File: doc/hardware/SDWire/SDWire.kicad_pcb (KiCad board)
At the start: 2 copper layers, 21.6 x 48.4 mm, 82 parts, among them J1 usd-plug, J2 uSD Socket, P1 USB_OTG_MICRO_USB, Q3 MMBT4403LT1, Q4 MMBT4403LT1, U1 USB2640-HZH-02, U2 SPX3819M5, U3 FT200XD, U4 MC74HC1G04DTT1G, U5 TS3A27518EPWR, Y1 24MHz

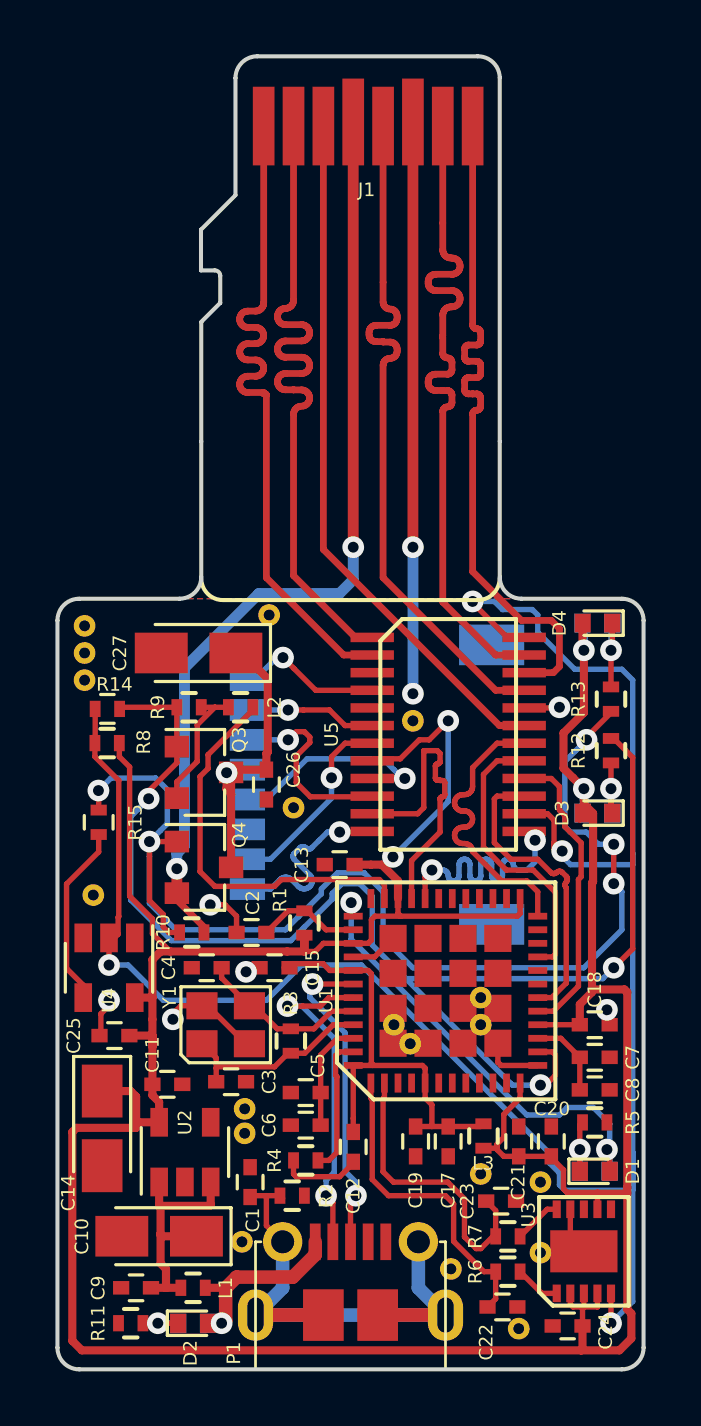
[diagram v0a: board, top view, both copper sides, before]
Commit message: Fix LEDs and card detect connections
Change-Id: I041ff52d267cebffd98fdaa6a1c2b5b6e2d7bece
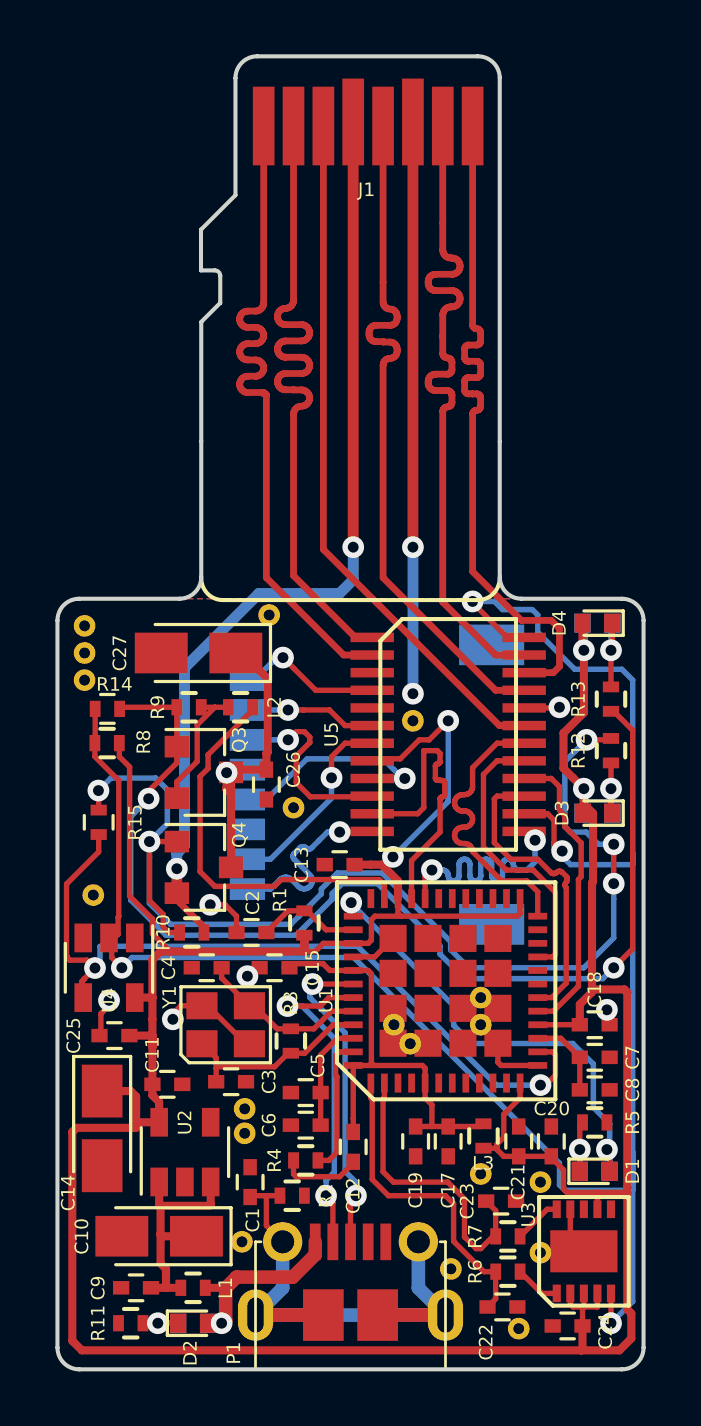
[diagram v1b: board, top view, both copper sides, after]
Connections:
- Q3 pad 1: /~CD_TS -> Net-(Q3-Pad1)
- R12 pad 2: /~CD_TS -> Net-(Q4-Pad1)
- R13 pad 2: Net-(Q4-Pad1) -> Net-(Q3-Pad1)
- R14 pad 1: /~CD_TS -> Net-(Q3-Pad1)
- R15 pad 2: Net-(R15-Pad2) -> /~CD_TS
- R9 pad 1: /~CD_TS -> Net-(Q3-Pad1)
- U4 pad 4: Net-(R15-Pad2) -> /~CD_TS
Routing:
- net Net-(Q3-Pad1): track 0.00 -> 41.2 mm, vias 0 -> 2
- net /~CD_TS: track 49.9 -> 29.4 mm, vias 3 -> 2
- net Net-(R15-Pad2): track 6.76 -> 0.00 mm
- net Net-(Q4-Pad1): track 45.4 -> 43.7 mm
- net /SOCKET_SEL: track 77.3 -> 76.3 mm
